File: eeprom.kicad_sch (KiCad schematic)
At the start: 9 parts, among them J19 WP Jumper, U9 AT24C64D

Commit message: quiet some kibot complaints
space at end of property value
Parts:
- R10, R11, R12, R13, R14, R15: Manufacturer Yageo -> Yageo
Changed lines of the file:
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@@
 			)
 		)
-		(property "Manufacturer" "Yageo "
+		(property "Manufacturer" "Yageo"
 			(at 105.41 99.06 0)
 			(effects
@@
 			)
 		)
-		(property "Manufacturer" "Yageo "
+		(property "Manufacturer" "Yageo"
 			(at 151.13 90.17 0)
 			(effects
@@
 			)
 		)
-		(property "Manufacturer" "Yageo "
+		(property "Manufacturer" "Yageo"
 			(at 167.64 93.98 0)
 			(effects
@@
 			)
 		)
-		(property "Manufacturer" "Yageo "
+		(property "Manufacturer" "Yageo"
 			(at 121.92 104.14 0)
 			(effects
@@
 			)
 		)
-		(property "Manufacturer" "Yageo "
+		(property "Manufacturer" "Yageo"
 			(at 115.57 101.6 0)
 			(effects
@@
 			)
 		)
-		(property "Manufacturer" "Yageo "
+		(property "Manufacturer" "Yageo"
 			(at 175.26 93.98 0)
 			(effects

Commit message: Updated Supplier part numbers
Updated Supplier part number for parts with incorrect or missing info
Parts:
- R10, R11, R12, R14, R15: Supplier Part Number 311-4.42KHRCT-ND -> 13-RC0603FR-134K75LCT-ND
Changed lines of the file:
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@@
 			)
 		)
-		(property "Supplier Part Number" "311-4.42KHRCT-ND"
+		(property "Supplier Part Number" "13-RC0603FR-134K75LCT-ND"
 			(at 105.41 99.06 90)
 			(effects
@@
 			)
 		)
-		(property "Supplier Part Number" "311-4.42KHRCT-ND"
+		(property "Supplier Part Number" "13-RC0603FR-134K75LCT-ND"
 			(at 167.64 93.98 0)
 			(effects
@@
 			)
 		)
-		(property "Supplier Part Number" "311-4.42KHRCT-ND"
+		(property "Supplier Part Number" "13-RC0603FR-134K75LCT-ND"
 			(at 121.92 104.14 90)
 			(effects
@@
 			)
 		)
-		(property "Supplier Part Number" "311-4.42KHRCT-ND"
+		(property "Supplier Part Number" "13-RC0603FR-134K75LCT-ND"
 			(at 115.57 101.6 90)
 			(effects
@@
 			)
 		)
-		(property "Supplier Part Number" "311-4.42KHRCT-ND"
+		(property "Supplier Part Number" "13-RC0603FR-134K75LCT-ND"
 			(at 175.26 93.98 0)
 			(effects

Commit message: Prototype Production Ready
- Removed Supplier and Supplier Part Numbers for project
- Changed Kibot to not out Supplier and Supplier Part Numbers for project
- Changed a few ignored ERC/DRC testing to warnings, and found no additional issues
- project is ready for production
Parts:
- C33: Supplier Digikey -> (none); Supplier Part Number 490-10673-1-ND -> (none)
- J19: Supplier Digikey -> (none); Supplier Part Number 952-2261-ND -> (none)
- R10, R11, R12, R14, R15: Supplier Digikey -> (none); Supplier Part Number 13-RC0603FR-134K75LCT-ND -> (none)
- R13: Supplier Digikey -> (none); Supplier Part Number 311-11.5KHRCT-ND -> (none)
- U9: Supplier Digikey -> (none); Supplier Part Number AT24C64D-SSHM-TCT-ND -> (none)
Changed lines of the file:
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@@
-			)
-		)
-		(property "Supplier" "Digikey"
-			(at 105.41 99.06 90)
-			(effects
-				(font
-					(size 1.27 1.27)
-				)
-				(hide yes)
-			)
-		)
-		(property "Supplier Part Number" "13-RC0603FR-134K75LCT-ND"
-			(at 105.41 99.06 90)
-			(effects
-				(font
-					(size 1.27 1.27)
-				)
-				(hide yes)
 			)
 		)
@@
 			)
 		)
-		(property "Supplier" "Digikey"
-			(at 151.13 90.17 0)
-			(effects
-				(font
-					(size 1.27 1.27)
-				)
-				(hide yes)
-			)
-		)
-		(property "Supplier Part Number" "311-11.5KHRCT-ND"
-			(at 151.13 90.17 0)
-			(effects
-				(font
-					(size 1.27 1.27)
-				)
-				(hide yes)
-			)
-		)
 		(pin "1"
 		)
@@
 			)
 		)
-		(property "Supplier" "Digikey"
-			(at 138.43 101.6 0)
-			(effects
-				(font
-					(size 1.27 1.27)
-				)
-				(hide yes)
-			)
-		)
-		(property "Supplier Part Number" "AT24C64D-SSHM-TCT-ND"
-			(at 138.43 101.6 0)
-			(effects
-				(font
-					(size 1.27 1.27)
-				)
-				(hide yes)
-			)
-		)
 		(pin "1"
 		)
@@
 			)
 		)
-		(property "Supplier" "Digikey"
-			(at 133.35 86.36 0)
-			(effects
-				(font
-					(size 1.27 1.27)
-				)
-				(hide yes)
-			)
-		)
-		(property "Supplier Part Number" "490-10673-1-ND"
-			(at 133.35 86.36 0)
-			(effects
-				(font
-					(size 1.27 1.27)
-				)
-				(hide yes)
-			)
-		)
 		(pin "1"
 		)
@@
 			)
 		)
-		(property "Supplier" "Digikey"
-			(at 167.64 93.98 0)
-			(effects
-				(font
-					(size 1.27 1.27)
-				)
-				(hide yes)
-			)
-		)
-		(property "Supplier Part Number" "13-RC0603FR-134K75LCT-ND"
-			(at 167.64 93.98 0)
-			(effects
-				(font
-					(size 1.27 1.27)
-				)
-				(hide yes)
-			)
-		)
 		(pin "1"
 		)
@@
 			)
 		)
-		(property "Supplier" "Digikey"
-			(at 121.92 104.14 90)
-			(effects
-				(font
-					(size 1.27 1.27)
-				)
-				(hide yes)
-			)
-		)
-		(property "Supplier Part Number" "13-RC0603FR-134K75LCT-ND"
-			(at 121.92 104.14 90)
-			(effects
-				(font
-					(size 1.27 1.27)
-				)
-				(hide yes)
-			)
-		)
 		(pin "1"
 		)
@@
 			)
 		)
-		(property "Supplier" "Digikey"
-			(at 115.57 101.6 90)
-			(effects
-				(font
-					(size 1.27 1.27)
-				)
-				(hide yes)
-			)
-		)
-		(property "Supplier Part Number" "13-RC0603FR-134K75LCT-ND"
-			(at 115.57 101.6 90)
-			(effects
-				(font
-					(size 1.27 1.27)
-				)
-				(hide yes)
-			)
-		)
 		(pin "1"
 		)
@@
 			)
 		)
-		(property "Supplier" "Digikey"
-			(at 161.29 107.95 0)
-			(effects
-				(font
-					(size 1.27 1.27)
-				)
-				(hide yes)
-			)
-		)
-		(property "Supplier Part Number" "952-2261-ND"
-			(at 161.29 107.95 0)
-			(effects
-				(font
-					(size 1.27 1.27)
-				)
-				(hide yes)
-			)
-		)
 		(pin "1"
 		)
@@
 			(at 175.26 93.98 0)
 			(effects
-				(font
-					(size 1.27 1.27)
-				)
-				(hide yes)
-			)
-		)
-		(property "Supplier" "Digikey"
-			(at 175.26 93.98 0)
-			(effects
-				(font
-					(size 1.27 1.27)
-				)
-				(hide yes)
-			)
-		)
-		(property "Supplier Part Number" "13-RC0603FR-134K75LCT-ND"
-			(at 175.26 93.98 0)
-			(effects

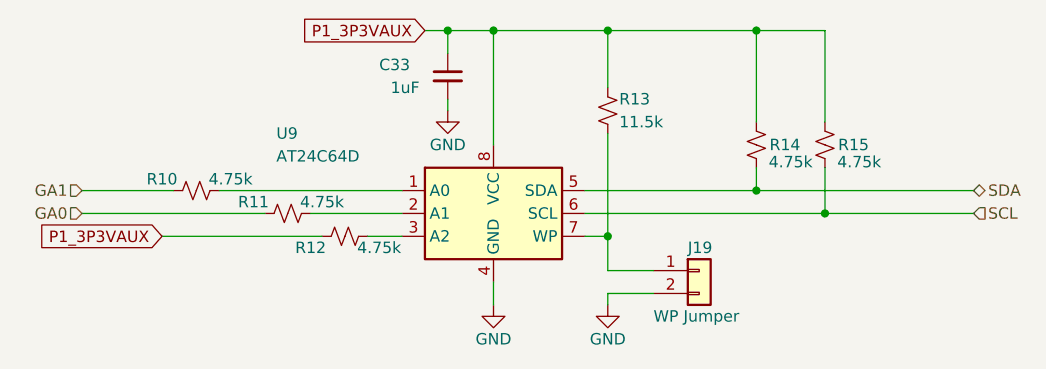
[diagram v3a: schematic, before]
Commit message: Updates based on Review
-Added Missing "PG_C2M" label
-Added heartbeat signal to fmc (was missing on previous commit)
-Changed all vias to 0.6mm with 0.3mm hole
	-Adjusted one via near pin7 of U7 to accommodate this change
-Changed traces around U4 to R25 to keep trace straight
-Added GND via at pin5 of U7 & connected all GND pins of U7 to PAD
-Moved R9 near J16 connector
-Changed name of board on silkscreen to "Clock Input FMC" project/file name changes will come in later commits.
-Standardized "J*" labels to all be consistent
-Swapped FMC pins for Din14 & Din15. This undoes some complications in the last commit with pin swaps
-Removed net references to "P1_" in net names
-Adjusted plane layers keepout and min width to be more consistent
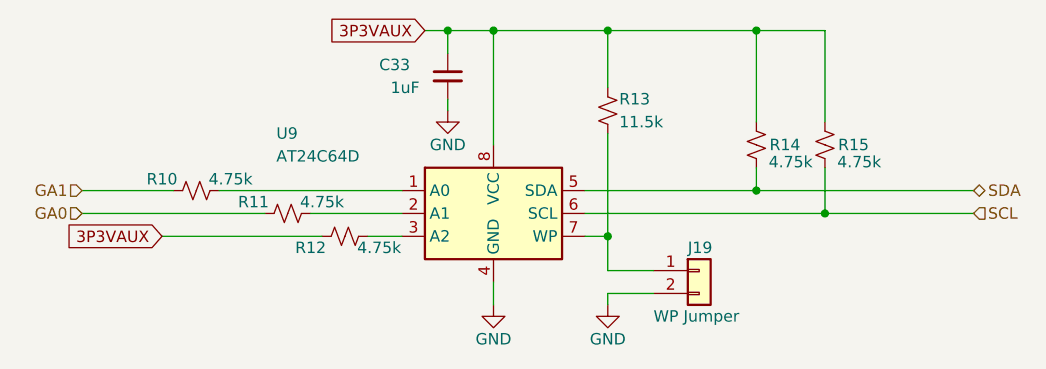
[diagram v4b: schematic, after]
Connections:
- net P1_3P3VAUX renamed 3P3VAUX
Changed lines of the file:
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@@
 		)
 	)
-	(global_label "P1_3P3VAUX"
+	(global_label "3P3VAUX"
 		(shape input)
 		(at 130.81 81.28 180)
@@
 		)
 		(property "Intersheetrefs" "${INTERSHEET_REFS}"
-			(at 116.0509 81.28 0)
+			(at 119.4186 81.28 0)
 			(effects
 				(font
@@
 		)
 	)
-	(global_label "P1_3P3VAUX"
+	(global_label "3P3VAUX"
 		(shape input)
 		(at 101.6 104.14 180)
@@
 		)
 		(property "Intersheetrefs" "${INTERSHEET_REFS}"
-			(at 86.7615 104.14 0)
+			(at 90.2086 104.14 0)
 			(effects
 				(font

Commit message: Changed Title Blocks to Version 1.0
- changed title blocks
- changed silkscreen to add version number
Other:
- title: RF Input FMC Board -> Clock Input FMC Board
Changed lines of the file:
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@@
 	(paper "USLetter")
 	(title_block
-		(title "RF Input FMC Board")
-		(date "2025-10-16")
-		(rev "0.2")
+		(title "Clock Input FMC Board")
+		(date "2026-05-20")
+		(rev "1.0")
 		(company "SPDX-FileCopyrightText: 2025 Osprey DCS")
 		(comment 1 "SPDX-License-Identifier: CERN-OHL-S-2.0+")
